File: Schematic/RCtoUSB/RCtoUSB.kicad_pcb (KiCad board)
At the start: 2 copper layers, 48 x 66.8 mm, 39 parts, among them J1 Power, J2 PORTA, J3 SAT, J4 ICSP, J5 PORTB, J6 USB_B_Mini, J7 USB_B_Mini, J8 SAT, J9 ICSP, Q1 2N7002P_215, Q2 2N7002P_215, U1 AP2210N-3.3TRG1, U2 PIC18f27J53, U3 AP2210N-3.3TRG1, U4 pic18lf27j53-i_ml

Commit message: Finished schematic and pcb
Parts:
- moved C1 54.8 mm to (112.5, 98.0)
- moved C2 54.8 mm to (93.5, 83.5)
- moved C3 54.8 mm to (116.2, 93.5)
- moved C4 54.8 mm to (110.2, 86.8)
- moved C5 54.8 mm to (112.8, 116.0)
- moved C7 54.8 mm to (117.2, 119.2)
- moved C8 54.8 mm to (106.0, 113.8)
- moved D1 54.8 mm to (84.5, 89.2)
- moved D2 54.8 mm to (84.6, 94.0)
- moved D3 54.8 mm to (117.0, 125.8)
- moved D4 54.8 mm to (117.0, 122.8)
- moved J1 54.8 mm to (89.5, 67.5)
- moved J2 54.8 mm to (86.8, 73.2)
- moved J3 54.8 mm to (100.5, 98.8)
- moved J4 54.8 mm to (98.2, 67.2)
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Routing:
- net Net-(C6-Pad1): track 3.09 -> 2.01 mm
- net GND2: track 41.9 -> 40.9 mm
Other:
- net class Default: clearance 0.2 -> 0.127
- rule pad_to_mask_clearance: 0 -> 0.05
- rule trace_clearance: 0.2 -> 0.127

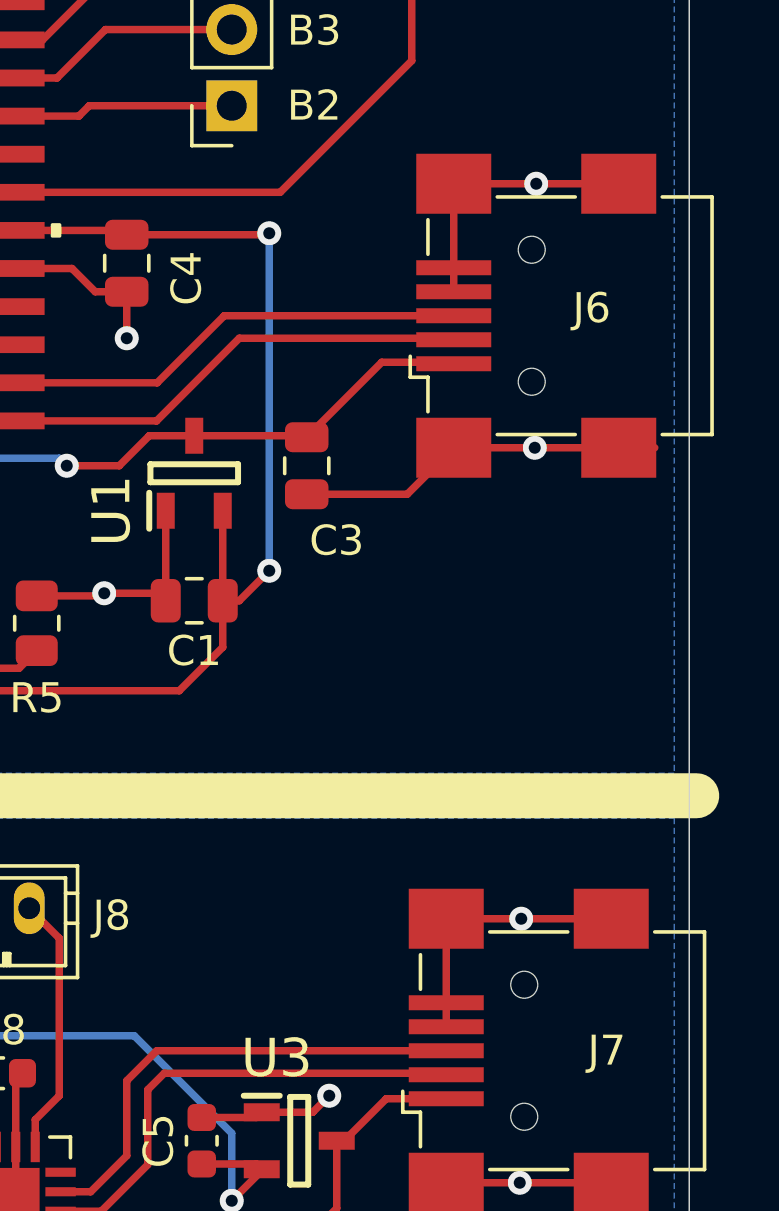
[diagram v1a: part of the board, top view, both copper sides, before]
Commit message: Changed ID pin to floating on USB connector
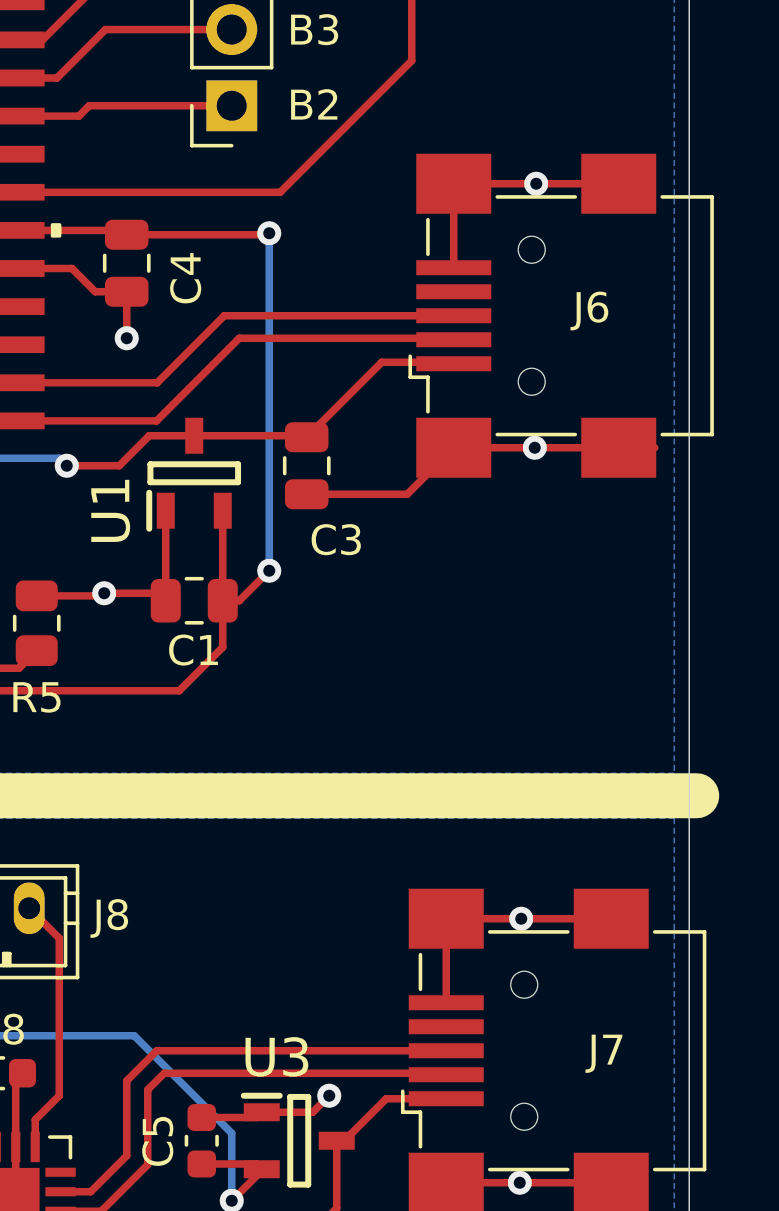
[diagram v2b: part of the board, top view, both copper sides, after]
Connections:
- J6 pad 4: GND1 -> Net-(J6-Pad4)
- J7 pad 4: GND2 -> Net-(J7-Pad4)
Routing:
- net GND1: track 48.8 -> 48.0 mm
- net GND2: track 40.9 -> 40.1 mm

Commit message: Converted to KiCad 6
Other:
- net class Default removed
